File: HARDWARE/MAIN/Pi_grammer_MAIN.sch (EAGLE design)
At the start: 57 parts, among them J3 RA 6Pin SMD, Q1 220mA/50V/3.5Ω, Q2 220mA/50V/3.5Ω, Q3 220mA/50V/3.5Ω, Q4 220mA/50V/3.5Ω, Q5 220mA/50V/3.5Ω, U1 AT42QT1010UDFN, U2 74LVC4066

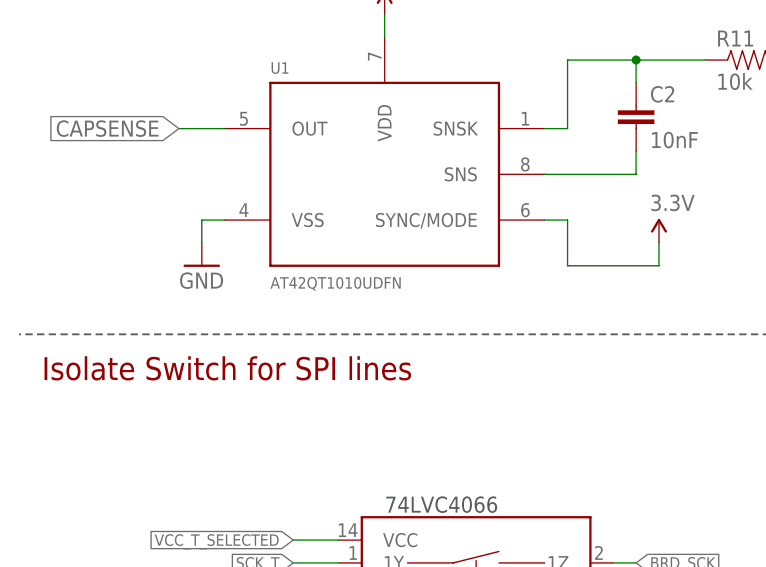
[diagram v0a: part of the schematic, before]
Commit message: updated AT42QT1010 to pull from the proper sparkfun eagle sensor library dev
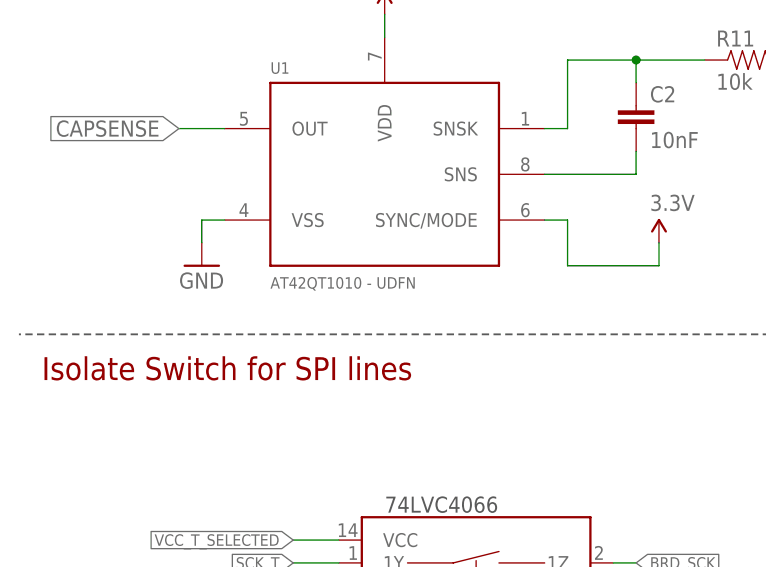
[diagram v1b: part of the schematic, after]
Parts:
- U1: value AT42QT1010UDFN -> AT42QT1010 - UDFN; device Testing:AT42QT1010UDFN -> SparkFun-Sensors:AT42QT1010UDFN
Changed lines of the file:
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@@
 <grid distance="0.1" unitdist="inch" unit="inch" style="lines" multiple="1" display="no" altdistance="0.01" altunitdist="inch" altunit="inch"/>
 <layers>
-<layer number="1" name="Top" color="4" fill="1" visible="yes" active="no"/>
-<layer number="2" name="Route2" color="1" fill="3" visible="yes" active="no"/>
-<layer number="3" name="Route3" color="4" fill="3" visible="yes" active="no"/>
-<layer number="4" name="Route4" color="1" fill="4" visible="yes" active="no"/>
-<layer number="5" name="Route5" color="4" fill="4" visible="yes" active="no"/>
-<layer number="6" name="Route6" color="1" fill="8" visible="yes" active="no"/>
-<layer number="7" name="Route7" color="4" fill="8" visible="yes" active="no"/>
-<layer number="8" name="Route8" color="1" fill="2" visible="yes" active="no"/>
-<layer number="9" name="Route9" color="4" fill="2" visible="yes" active="no"/>
-<layer number="10" name="Route10" color="1" fill="7" visible="yes" active="no"/>
-<layer number="11" name="Route11" color="4" fill="7" visible="yes" active="no"/>
-<layer number="12" name="Route12" color="1" fill="5" visible="yes" active="no"/>
-<layer number="13" name="Route13" color="4" fill="5" visible="yes" active="no"/>
-<layer number="14" name="Route14" color="1" fill="6" visible="yes" active="no"/>
-<layer number="15" name="Route15" color="4" fill="6" visible="yes" active="no"/>
-<layer number="16" name="Bottom" color="1" fill="1" visible="yes" active="no"/>
-<layer number="17" name="Pads" color="2" fill="1" visible="yes" active="no"/>
-<layer number="18" name="Vias" color="2" fill="1" visible="yes" active="no"/>
-<layer number="19" name="Unrouted" color="6" fill="1" visible="yes" active="no"/>
-<layer number="20" name="Dimension" color="15" fill="1" visible="yes" active="no"/>
-<layer number="21" name="tPlace" color="16" fill="1" visible="yes" active="no"/>
-<layer number="22" name="bPlace" color="14" fill="1" visible="yes" active="no"/>
-<layer number="23" name="tOrigins" color="15" fill="1" visible="yes" active="no"/>
-<layer number="24" name="bOrigins" color="15" fill="1" visible="yes" active="no"/>
-<layer number="25" name="tNames" color="7" fill="1" visible="yes" active="no"/>
-<layer number="26" name="bNames" color="7" fill="1" visible="yes" active="no"/>
-<layer number="27" name="tValues" color="7" fill="1" visible="yes" active="no"/>
-<layer number="28" name="bValues" color="7" fill="1" visible="yes" active="no"/>
+<layer number="1" name="Top" color="4" fill="1" visible="no" active="no"/>
+<layer number="2" name="Route2" color="1" fill="3" visible="no" active="no"/>
+<layer number="3" name="Route3" color="4" fill="3" visible="no" active="no"/>
+<layer number="4" name="Route4" color="1" fill="4" visible="no" active="no"/>
+<layer number="5" name="Route5" color="4" fill="4" visible="no" active="no"/>
+<layer number="6" name="Route6" color="1" fill="8" visible="no" active="no"/>
+<layer number="7" name="Route7" color="4" fill="8" visible="no" active="no"/>
+<layer number="8" name="Route8" color="1" fill="2" visible="no" active="no"/>
+<layer number="9" name="Route9" color="4" fill="2" visible="no" active="no"/>
+<layer number="10" name="Route10" color="1" fill="7" visible="no" active="no"/>
+<layer number="11" name="Route11" color="4" fill="7" visible="no" active="no"/>
+<layer number="12" name="Route12" color="1" fill="5" visible="no" active="no"/>
+<layer number="13" name="Route13" color="4" fill="5" visible="no" active="no"/>
+<layer number="14" name="Route14" color="1" fill="6" visible="no" active="no"/>
+<layer number="15" name="Route15" color="4" fill="6" visible="no" active="no"/>
+<layer number="16" name="Bottom" color="1" fill="1" visible="no" active="no"/>
+<layer number="17" name="Pads" color="2" fill="1" visible="no" active="no"/>
+<layer number="18" name="Vias" color="2" fill="1" visible="no" active="no"/>
+<layer number="19" name="Unrouted" color="6" fill="1" visible="no" active="no"/>
+<layer number="20" name="Dimension" color="15" fill="1" visible="no" active="no"/>
+<layer number="21" name="tPlace" color="16" fill="1" visible="no" active="no"/>
+<layer number="22" name="bPlace" color="14" fill="1" visible="no" active="no"/>
+<layer number="23" name="tOrigins" color="15" fill="1" visible="no" active="no"/>
+<layer number="24" name="bOrigins" color="15" fill="1" visible="no" active="no"/>
+<layer number="25" name="tNames" color="7" fill="1" visible="no" active="no"/>
+<layer number="26" name="bNames" color="7" fill="1" visible="no" active="no"/>
+<layer number="27" name="tValues" color="7" fill="1" visible="no" active="no"/>
+<layer number="28" name="bValues" color="7" fill="1" visible="no" active="no"/>
 <layer number="29" name="tStop" color="7" fill="3" visible="no" active="no"/>
 <layer number="30" name="bStop" color="7" fill="6" visible="no" active="no"/>
@@
 <layer number="35" name="tGlue" color="7" fill="4" visible="no" active="no"/>
 <layer number="36" name="bGlue" color="7" fill="5" visible="no" active="no"/>
-<layer number="37" name="tTest" color="7" fill="1" visible="yes" active="no"/>
-<layer number="38" name="bTest" color="7" fill="1" visible="yes" active="no"/>
+<layer number="37" name="tTest" color="7" fill="1" visible="no" active="no"/>
+<layer number="38" name="bTest" color="7" fill="1" visible="no" active="no"/>
 <layer number="39" name="tKeepout" color="4" fill="11" visible="no" active="no"/>
 <layer number="40" name="bKeepout" color="1" fill="11" visible="no" active="no"/>
@@
 <layer number="44" name="Drills" color="7" fill="1" visible="no" active="no"/>
 <layer number="45" name="Holes" color="7" fill="1" visible="no" active="no"/>
-<layer number="46" name="Milling" color="3" fill="1" visible="yes" active="no"/>
-<layer number="47" name="Measures" color="7" fill="1" visible="yes" active="no"/>
-<layer number="48" name="Document" color="7" fill="1" visible="yes" active="no"/>
-<layer number="49" name="Reference" color="13" fill="1" visible="yes" active="no"/>
-<layer number="50" name="dxf" color="7" fill="1" visible="yes" active="no"/>
-<layer number="51" name="tDocu" color="6" fill="1" visible="yes" active="no"/>
-<layer number="52" name="bDocu" color="7" fill="1" visible="yes" active="no"/>
-<layer number="53" name="tGND_GNDA" color="7" fill="9" visible="yes" active="no"/>
-<layer number="54" name="bGND_GNDA" color="1" fill="9" visible="yes" active="no"/>
-<layer number="56" name="wert" color="7" fill="1" visible="yes" active="no"/>
-<layer number="57" name="tCAD" color="7" fill="1" visible="yes" active="no"/>
-<layer number="59" name="tCarbon" color="7" fill="1" visible="yes" active="no"/>
-<layer number="60" name="bCarbon" color="7" fill="1" visible="yes" active="no"/>
+<layer number="46" name="Milling" color="3" fill="1" visible="no" active="no"/>
+<layer number="47" name="Measures" color="7" fill="1" visible="no" active="no"/>
+<layer number="48" name="Document" color="7" fill="1" visible="no" active="no"/>
+<layer number="49" name="Reference" color="13" fill="1" visible="no" active="no"/>
+<layer number="50" name="dxf" color="7" fill="1" visible="no" active="no"/>
+<layer number="51" name="tDocu" color="6" fill="1" visible="no" active="no"/>
+<layer number="52" name="bDocu" color="7" fill="1" visible="no" active="no"/>
+<layer number="53" name="tGND_GNDA" color="7" fill="9" visible="no" active="no"/>
+<layer number="54" name="bGND_GNDA" color="1" fill="9" visible="no" active="no"/>
+<layer number="56" name="wert" color="7" fill="1" visible="no" active="no"/>
+<layer number="57" name="tCAD" color="7" fill="1" visible="no" active="no"/>
+<layer number="59" name="tCarbon" color="7" fill="1" visible="no" active="no"/>
+<layer number="60" name="bCarbon" color="7" fill="1" visible="no" active="no"/>
 <layer number="90" name="Modules" color="5" fill="1" visible="yes" active="yes"/>
 <layer number="91" name="Nets" color="2" fill="1" visible="yes" active="yes"/>
@@
 <part name="D7" library="SparkFun-LED" deviceset="LED-GREEN" device="1206" value="GREEN"/>
 <part name="LOGO2" library="SparkFun-Aesthetics" deviceset="OSHW-LOGO" device="L" value="OSHW-LOGOL"/>
-<part name="U1" library="Testing" deviceset="AT42QT1010" device="UDFN">
+<part name="U1" library="SparkFun-Sensors" deviceset="AT42QT1010" device="UDFN" value="AT42QT1010 - UDFN">
 <attribute name="PROD_ID" value="IC-11778"/>
 </part>

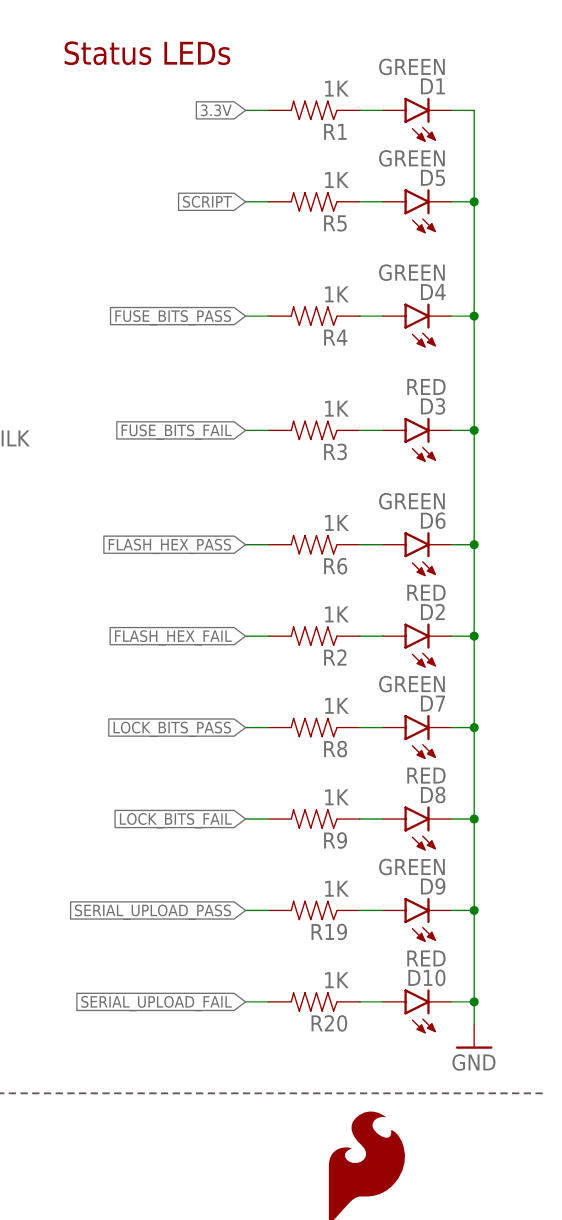
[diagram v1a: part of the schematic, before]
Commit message: updated switch (U2) to use sparkfun eagle library
also updated all libraries and the LEDs silk changed to updated versions of 1206 packages
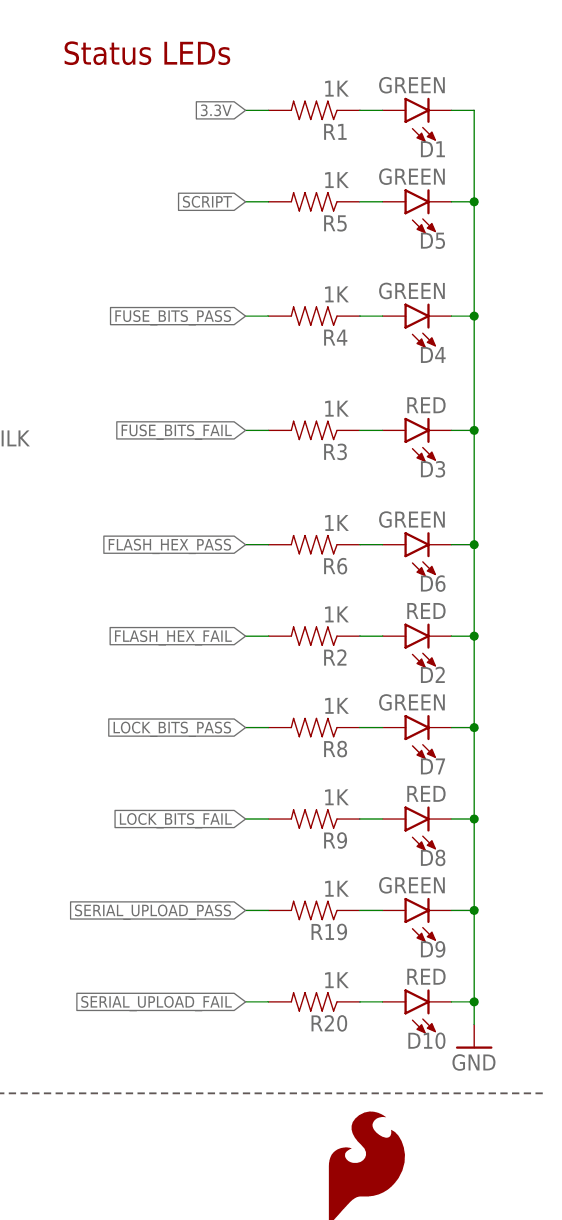
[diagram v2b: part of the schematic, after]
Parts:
- U2: device Testing:74LVC4066_MUX_1:1_X4 -> SparkFun-IC-Logic:74LVC4066D_QUAD_BILATERAL_SWITCH
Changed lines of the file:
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@@
 <part name="C7" library="SparkFun-Capacitors" deviceset="0.1UF" device="-0603-25V-(+80/-20%)" value="0.1uF"/>
 <part name="GND10" library="SparkFun" deviceset="GND" device=""/>
-<part name="U2" library="Testing" deviceset="74LVC4066_MUX_1:1_X4" device="" value="74LVC4066">
+<part name="U2" library="SparkFun-IC-Logic" deviceset="74LVC4066D_QUAD_BILATERAL_SWITCH" device="" value="74LVC4066">
 <attribute name="PROD_ID" value="IC-13944"/>
 </part>

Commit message: RA SMD 6 pin header updated to have correct prod ID
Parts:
- J3: PROD_ID CONN-10140 -> (none)
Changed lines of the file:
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@@
 <layer number="59" name="tCarbon" color="7" fill="1" visible="no" active="no"/>
 <layer number="60" name="bCarbon" color="7" fill="1" visible="no" active="no"/>
+<layer number="88" name="SimResults" color="9" fill="1" visible="no" active="yes"/>
+<layer number="89" name="SimProbes" color="9" fill="1" visible="no" active="yes"/>
 <layer number="90" name="Modules" color="5" fill="1" visible="yes" active="yes"/>
 <layer number="91" name="Nets" color="2" fill="1" visible="yes" active="yes"/>
@@
 </part>
 <part name="GND12" library="SparkFun" deviceset="GND" device=""/>
-<part name="J3" library="SparkFun-Connectors" deviceset="CONN_06" device="SMD" value="RA 6Pin SMD">
-<attribute name="PROD_ID" value="CONN-10140"/>
-</part>
+<part name="J3" library="SparkFun-Connectors" deviceset="CONN_06" device="SMD" value="RA 6Pin SMD"/>
 <part name="GND13" library="SparkFun-Aesthetics" deviceset="GND" device=""/>
 <part name="Q5" library="SparkFun-DiscreteSemi" deviceset="MOSFET-NCH" device="-BSS138" value="220mA/50V/3.5Ω"/>
